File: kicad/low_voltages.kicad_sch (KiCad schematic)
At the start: 6 parts, among them U401 TLV1117-33, U402 AP7363C-12E

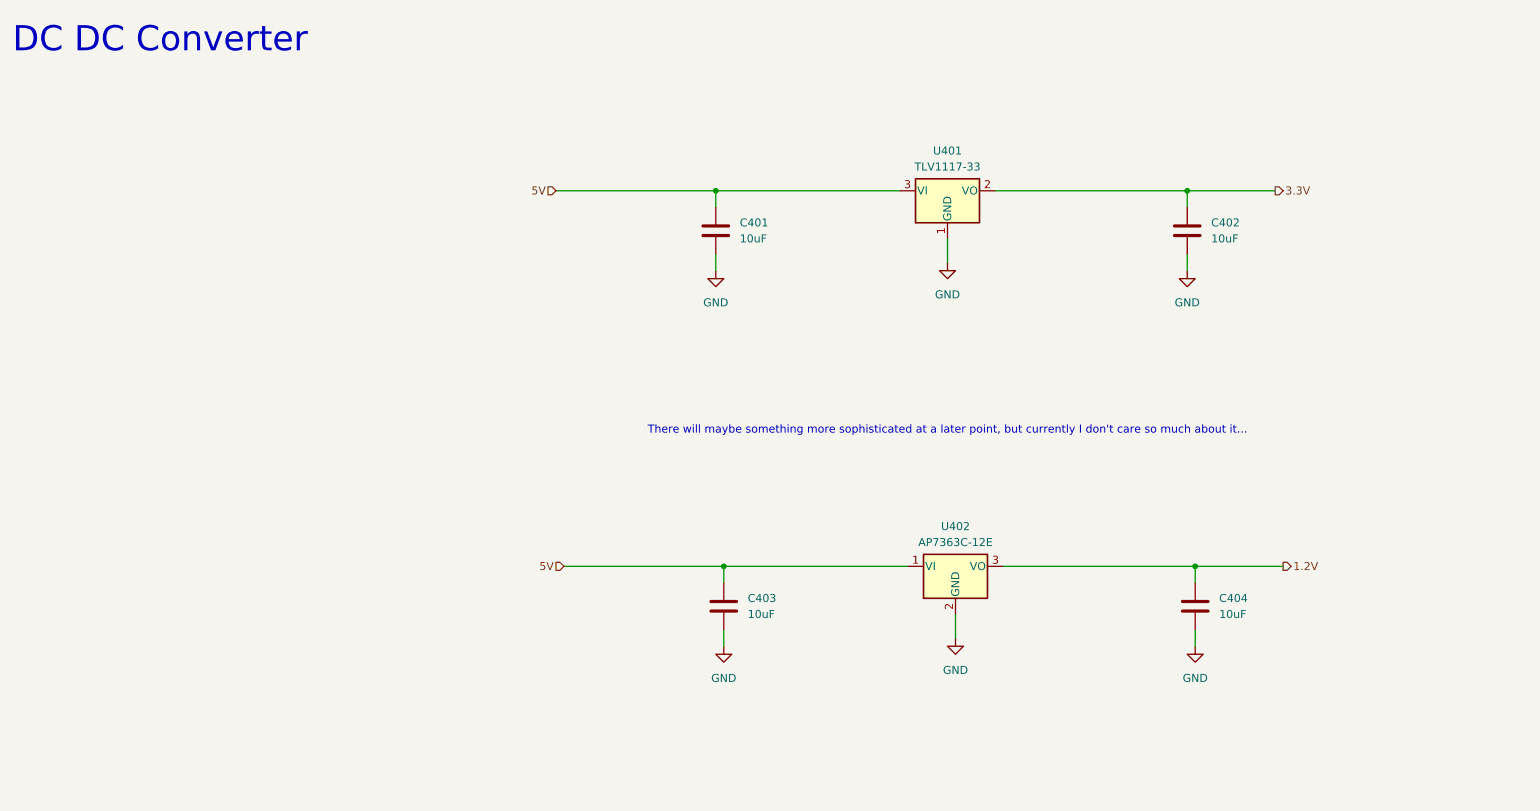
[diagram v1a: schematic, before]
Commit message: Replace 1.2V LDO with switching regulator
It just feels more reliable.
Also added 0R resistors between switch and alert signal. My hope is
that I can tell the switch to diable the port by pulling the
overcurrent low.
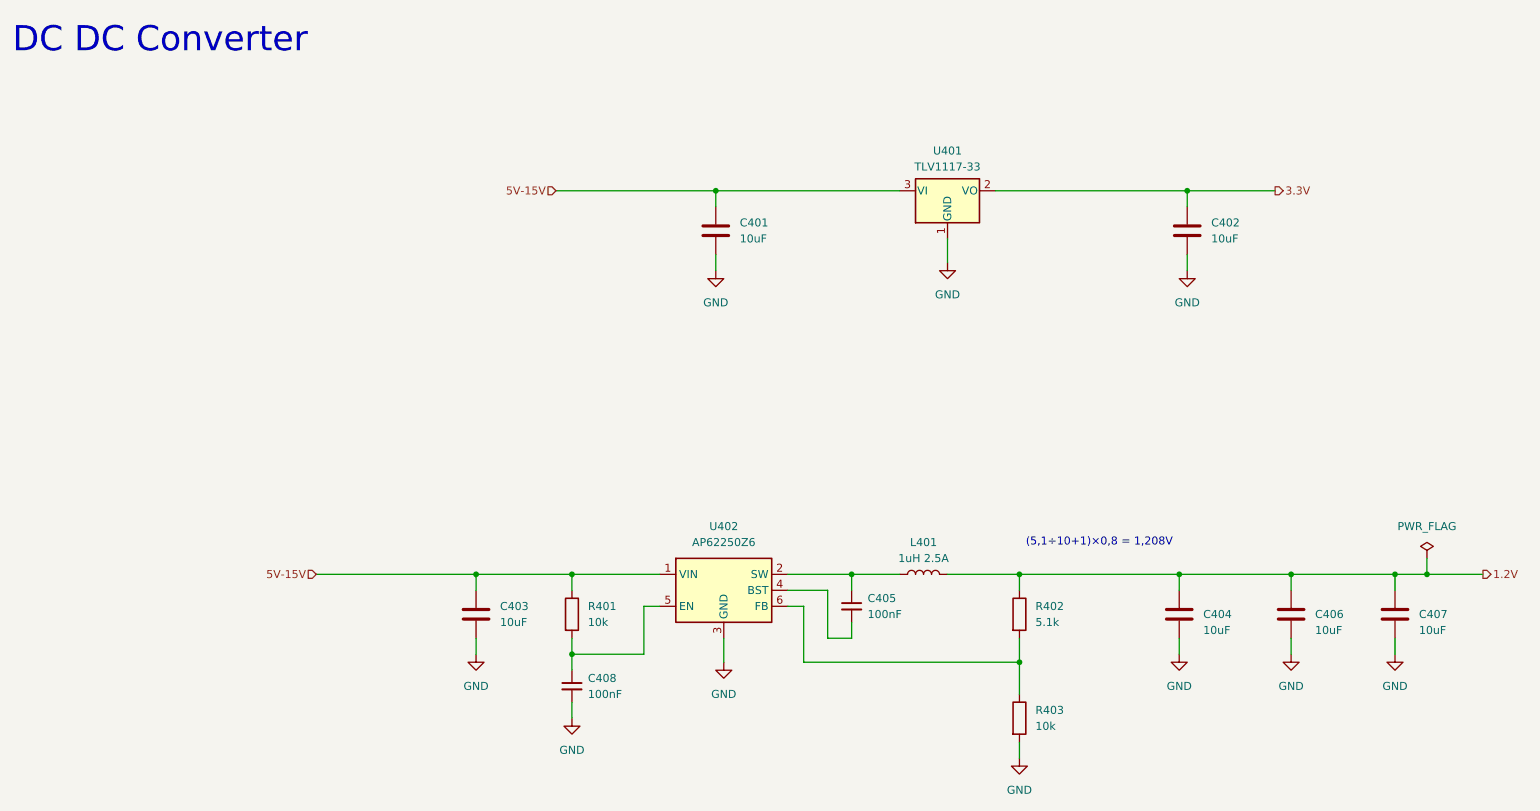
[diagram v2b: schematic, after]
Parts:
- removed U402: AP7363C-12E, Package_TO_SOT_SMD:SOT-223-3_TabPin2, symbol Regulator_Linear:AP7361C-12E
- added C405, C408: 100nF, Capacitor_SMD:C_0402_1005Metric, symbol Device:C_Small
- added C406, C407: 10uF, Capacitor_SMD:C_0805_2012Metric, symbol Device:C
- added L401: 1uH 2.5A, Inductor_SMD:L_Bourns-SRN4018, symbol Device:L
- added R401, R403: 10k, Resistor_SMD:R_0603_1608Metric, symbol Device:R
- added R402: 5.1k, Resistor_SMD:R_0603_1608Metric, symbol Device:R
- added U402: AP62250Z6, Package_TO_SOT_SMD:SOT-563, symbol Regulator_Switching:AP62250Z6
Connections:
- net 1.2V: now also C406.1, C407.1, L401.2, R402.1
- net GND: now also C406.2, C407.2, C408.2, R403.2, U402.3 (GND)
- net 5V renamed 5V-15V
- net 5V-15V: now also R401.1, U402.1 (VIN)
- new net: R402.2, R403.1, U402.6 (FB)
- new net: C405.1, L401.1, U402.2 (SW)
- new net: C405.2, U402.4 (BST)
- new net: C408.1, R401.2, U402.5 (EN)
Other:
- note added: "(5,1÷10+1)×0,8 = 1,208V"
- note removed: "There will maybe something more sophisticated at a later point, but currently I don't care so much about it..."
- moved on the sheet: C403, C404
